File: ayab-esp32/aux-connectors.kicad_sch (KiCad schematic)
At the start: 31 parts, among them J403 AYAB_I2C, J403 USER_I2C, J403 USER_UART, J404 AYAB_SPI, J404 USER_SPI

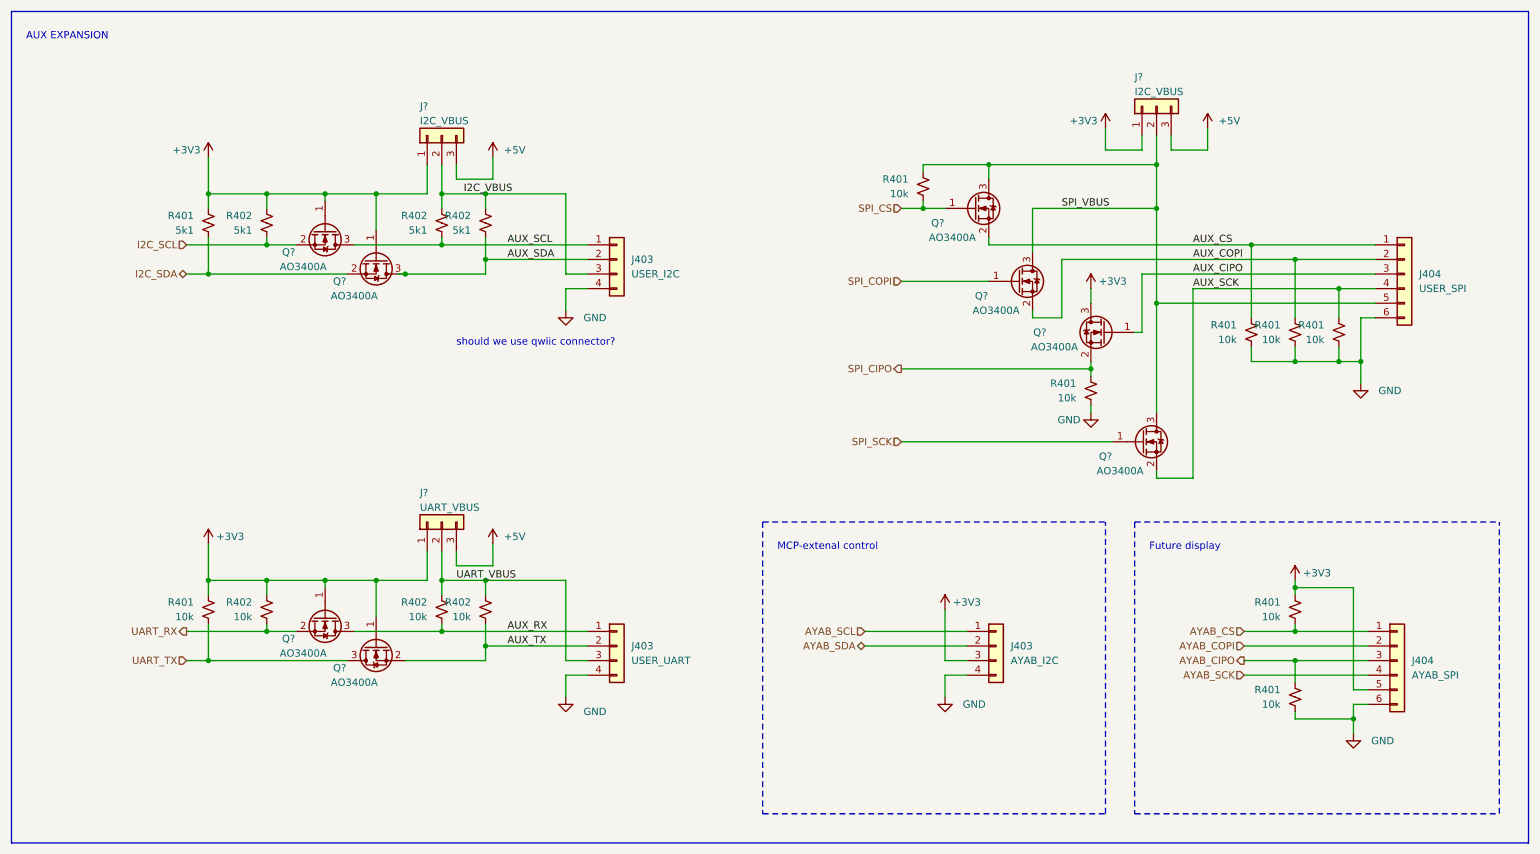
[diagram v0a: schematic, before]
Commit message: annotate and terminating resistors
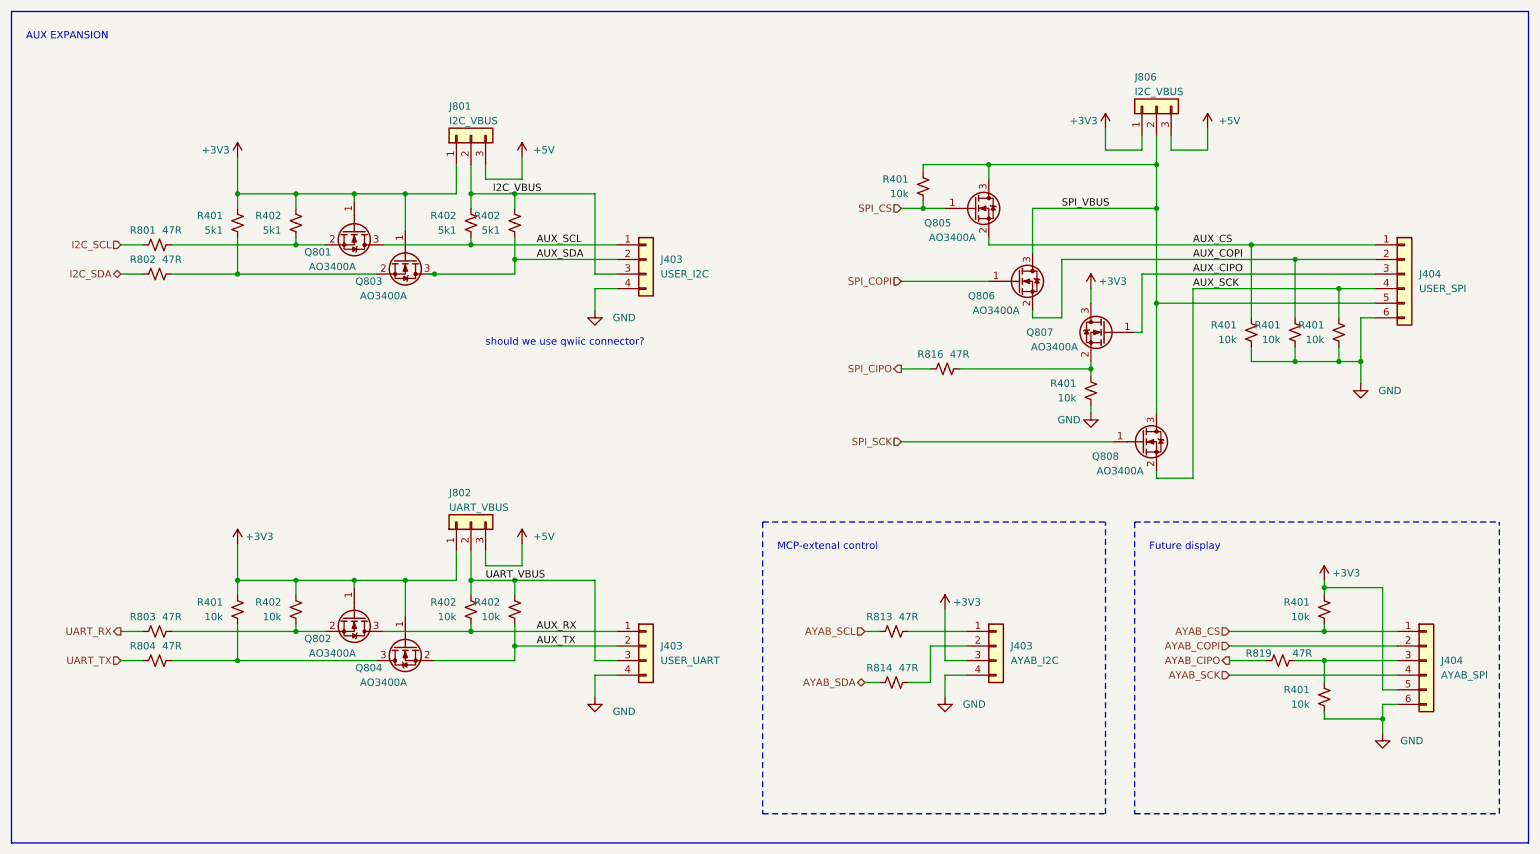
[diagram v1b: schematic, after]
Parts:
- added R801, R802, R803, R804, R813, R814, R816, R819: 47R, symbol ayab-esp32:R_Small_US
- gave numbers to parts that had none: 11
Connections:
- net AYAB_CIPO: now also R819.1; no longer J404.3 (Pin_3), R401.1
- net AYAB_SCL: now also R813.1; no longer J403.1 (Pin_1)
- net AYAB_SDA: now also R814.1; no longer J403.2 (Pin_2)
- net I2C_SCL: now also R801.1; no longer Q801.2 (S), R402.2
- net I2C_SDA: now also R802.1; no longer Q803.2 (S), R401.2
- net SPI_CIPO: now also R816.1; no longer Q807.2 (S), R401.1
- net UART_RX: now also R803.1; no longer Q802.2 (S), R402.2
- net UART_TX: now also R804.1; no longer Q804.3 (D), R401.2
- new net: Q802.2 (S), R402.2, R803.2
- new net: J404.3 (Pin_3), R401.1, R819.2
- new net: Q807.2 (S), R401.1, R816.2
- new net: J403.1 (Pin_1), R813.2
- new net: Q804.3 (D), R401.2, R804.2
- new net: J403.2 (Pin_2), R814.2
- new net: Q801.2 (S), R402.2, R801.2
- new net: Q803.2 (S), R401.2, R802.2
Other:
- moved on the sheet: J403, J404, J801, J802, Q801, Q802, Q803, Q804, R401, R402

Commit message: finalize external connectors
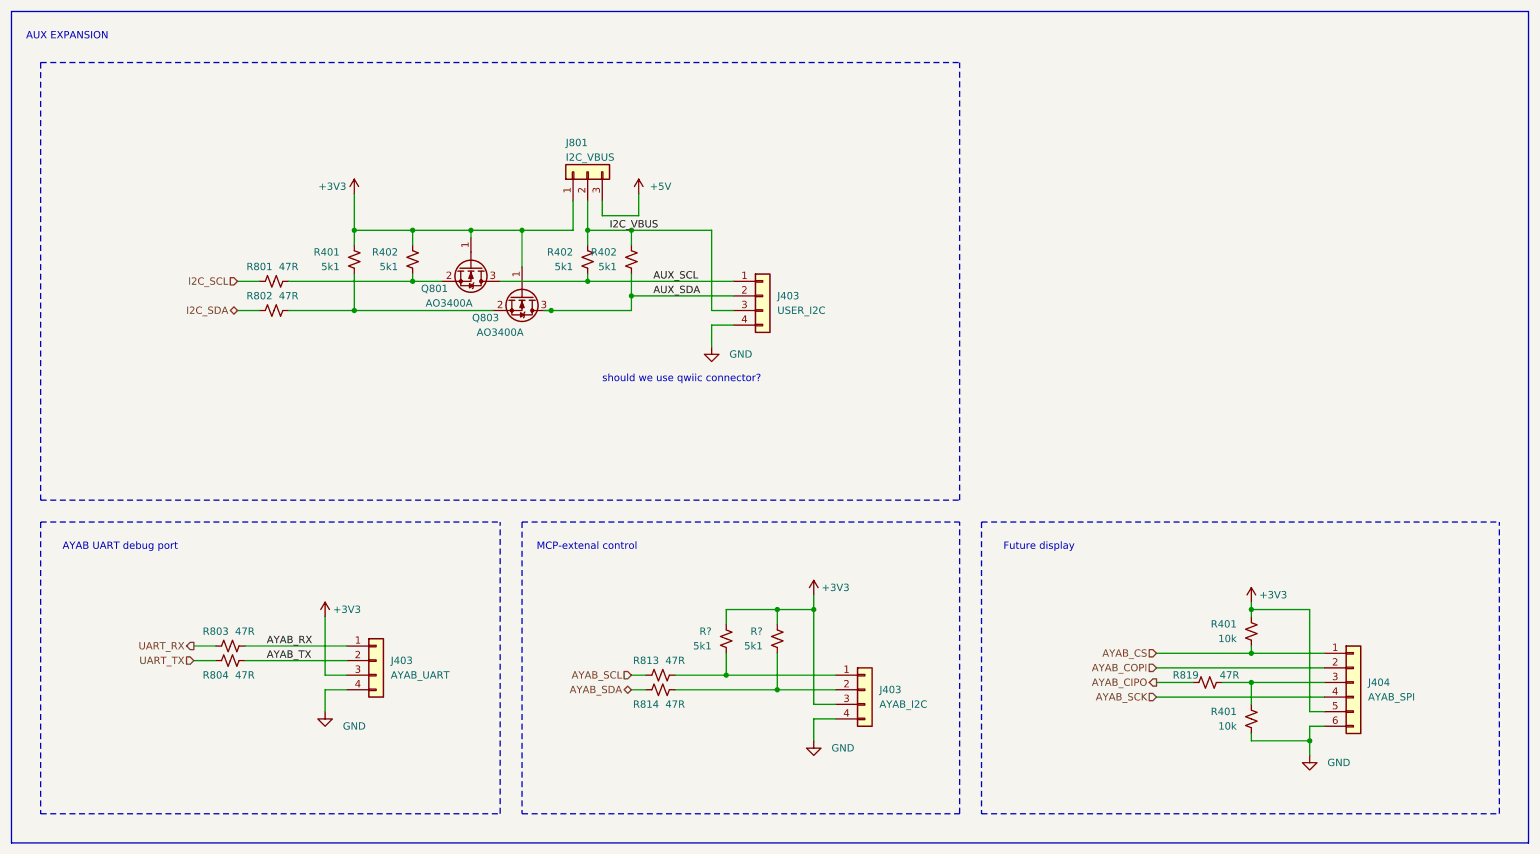
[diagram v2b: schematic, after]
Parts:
- removed J404: USER_SPI, symbol ayab-esp32:Conn_01x06
- removed J802: UART_VBUS, symbol Connector_Generic:Conn_01x03
- removed J806: I2C_VBUS, symbol Connector_Generic:Conn_01x03
- removed Q802, Q804, Q805, Q806, Q807, Q808: AO3400A, Package_TO_SOT_SMD:SOT-23, symbol ayab-esp32:AO3400A
- removed R401 (x6), R402 (x3): 10k, symbol ayab-esp32:R_Small_US
- removed R816: 47R, symbol ayab-esp32:R_Small_US
- added R? (x2): 5k1, symbol ayab-esp32:R_Small_US
- J403: value USER_UART -> AYAB_UART
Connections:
- net AUX_RX is gone; now on net AYAB_RX: J403.1 (Pin_1)
- net UART_VBUS is gone; now on net +3V3: J403.3 (Pin_3)
- net +3V3: now also R?.1, R?.1
- net AYAB_SDA: now also R814.2; no longer R814.1
- net UART_TX: now also R804.2; no longer R804.1
- net AYAB_RX: now reaches R803.2
- net at J403.1 (Pin_1), R813.2: now also R?.2
- net at J403.2 (Pin_2): now also R814.1, R?.2; no longer R814.2
- net AUX_TX renamed AYAB_TX
- net AYAB_TX: now also R804.1
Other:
- note added: "AYAB UART debug port"
- moved on the sheet: J403, J404, J801, Q801, Q803, R401, R402, R801, R802, R803, R804, R813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

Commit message: update local library + pdf
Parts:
- J802: renamed from J801; symbol Connector_Generic:Conn_01x03 -> ayab-esp32:Conn_01x03
- gave numbers to parts that had none: 2
- renumbered Q803 to Q802, R803 to R801, R804 to R802, R801 to R803, R802 to R804, R813 to R809, R814 to R810, R819 to R813

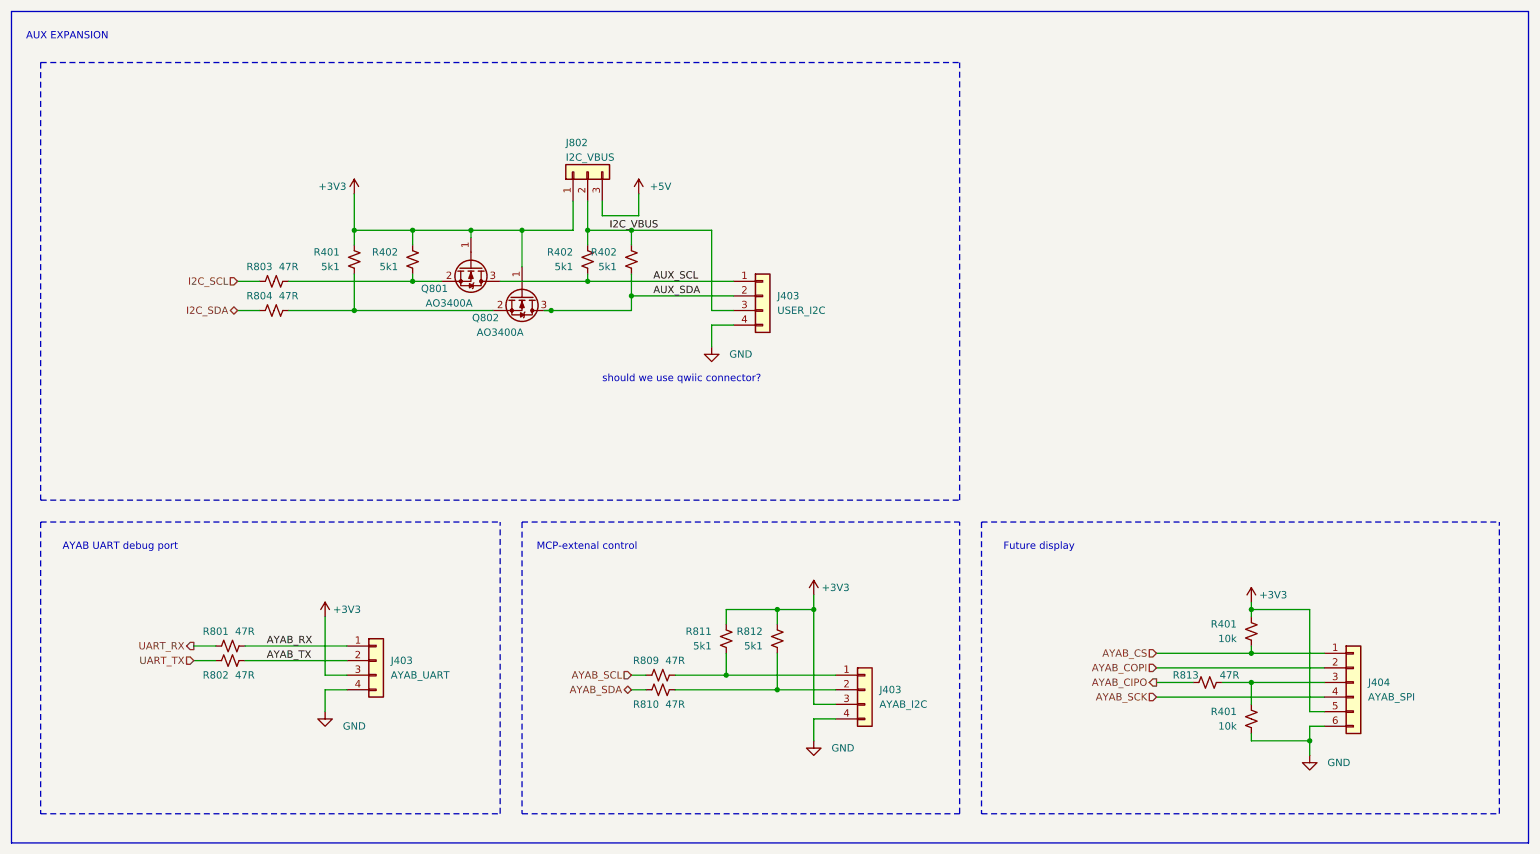
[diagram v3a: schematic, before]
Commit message: add component selection, bom
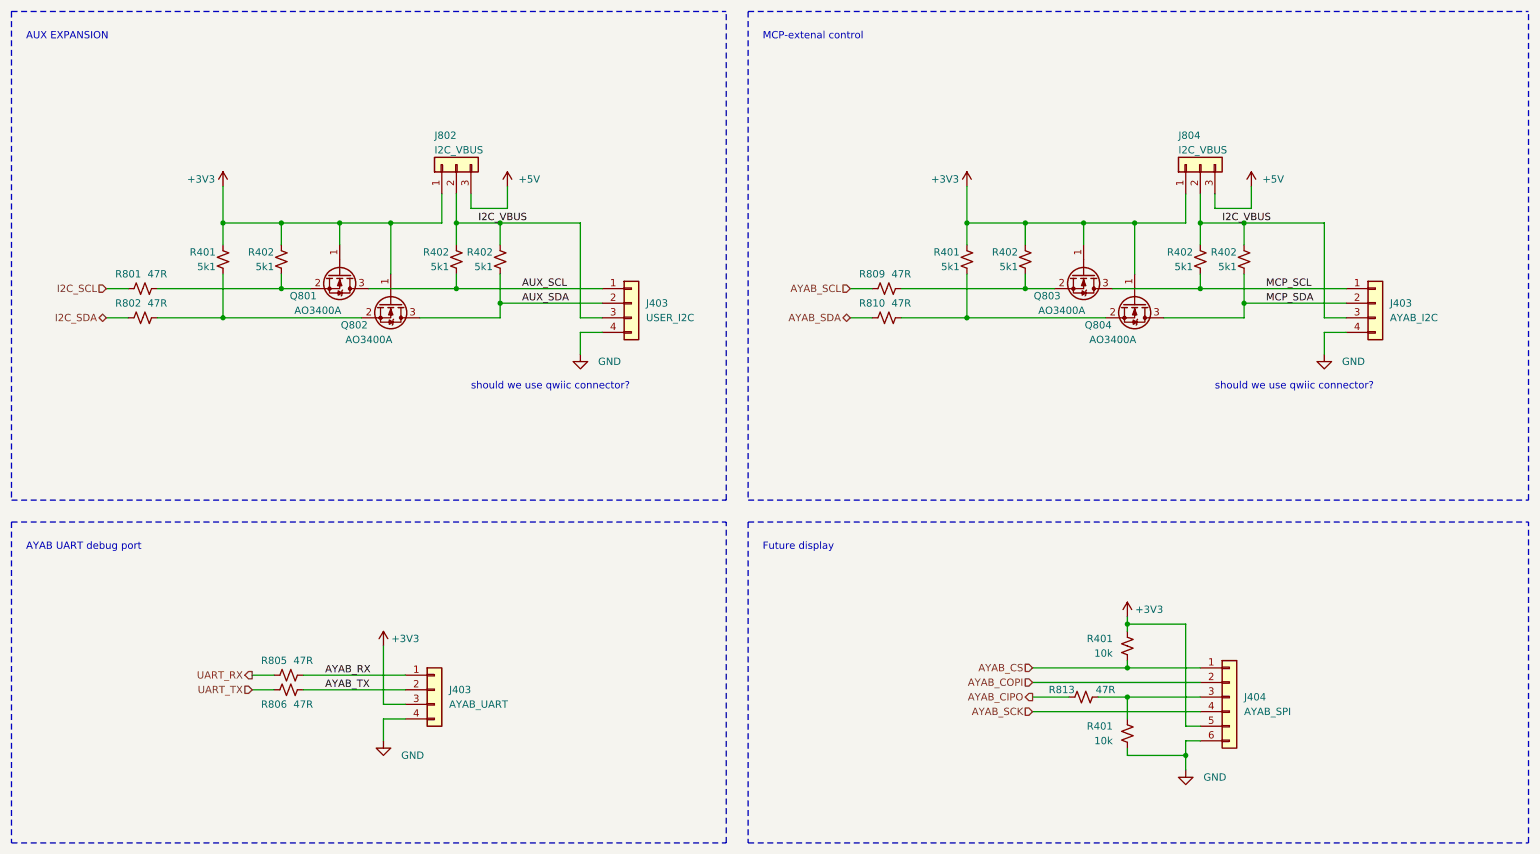
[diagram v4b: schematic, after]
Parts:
- removed R809, R810: 47R, symbol ayab-esp32:R_Small_US
- removed R811, R812: 5k1, symbol ayab-esp32:R_Small_US
- added J804: I2C_VBUS, Jumper:SolderJumper-3_P1.3mm_Bridged12_RoundedPad1.0x1.5mm, symbol Library:Conn_01x03
- added Q803, Q804: AO3400A, Package_TO_SOT_SMD:SOT-23, symbol Library:AO3400A
- added R401, R402 (x3): 5k1, Resistor_SMD:R_0603_1608Metric, symbol Library:R_Small_US
- added R809, R810: 47R, Resistor_SMD:R_0603_1608Metric, symbol Library:R_Small_US
- J403: footprint (none) -> Connector_PinHeader_2.54mm:PinHeader_1x04_P2.54mm_Vertical; symbol ayab-esp32:Conn_01x04 -> Library:Conn_01x04; LCSC ID (none) -> C3029334; OEM (none) -> XUNPU; OEM PN (none) -> WAFER-SH1.0-4PLB
- J403: footprint (none) -> Connector_JST:JST_SH_SM04B-SRSS-TB_1x04-1MP_P1.00mm_Horizontal; symbol ayab-esp32:Conn_01x04 -> Library:Conn_01x04; LCSC ID (none) -> C3029334; OEM (none) -> XUNPU; OEM PN (none) -> WAFER-SH1.0-4PLB
- J403: footprint (none) -> Connector_PinSocket_2.54mm:PinSocket_1x04_P2.54mm_Vertical; symbol ayab-esp32:Conn_01x04 -> Library:Conn_01x04; LCSC ID (none) -> C3029334; OEM (none) -> XUNPU; OEM PN (none) -> WAFER-SH1.0-4PLB
- J404: footprint (none) -> Connector_JST:JST_SH_SM06B-SRSS-TB_1x06-1MP_P1.00mm_Horizontal; symbol ayab-esp32:Conn_01x06 -> Library:Conn_01x06; LCSC ID (none) -> C3029345; OEM (none) -> XUNPU; OEM PN (none) -> WAFER-SH1.0-6PWB
- J802: footprint (none) -> Jumper:SolderJumper-3_P1.3mm_Bridged12_RoundedPad1.0x1.5mm; symbol ayab-esp32:Conn_01x03 -> Library:Conn_01x03
- Q801, Q802: symbol ayab-esp32:AO3400A -> Library:AO3400A; LCSC ID (none) -> C20917; OEM (none) -> Alpha & Omega Semicon; OEM PN (none) -> AO3400A; Package (none) -> SOT-23
- R401: footprint (none) -> Resistor_SMD:R_0603_1608Metric; symbol ayab-esp32:R_Small_US -> Library:R_Small_US; LCSC ID (none) -> C25804; OEM (none) -> UNI-ROYAL(Uniroyal Elec); OEM PN (none) -> 0603WAF1002T5E; Package (none) -> 0603
- R401, R402: footprint (none) -> Resistor_SMD:R_0603_1608Metric; symbol ayab-esp32:R_Small_US -> Library:R_Small_US; LCSC ID (none) -> C23186; OEM (none) -> UNI-ROYAL(Uniroyal Elec); OEM PN (none) -> 0603WAF5101T5E; Package (none) -> 0603
- R801: renamed from R803; footprint (none) -> Resistor_SMD:R_0603_1608Metric; symbol ayab-esp32:R_Small_US -> Library:R_Small_US; LCSC ID (none) -> C23182; OEM (none) -> UNI-ROYAL(Uniroyal Elec); OEM PN (none) -> 0603WAF470JT5E; Package (none) -> 0603
- R802: renamed from R804; footprint (none) -> Resistor_SMD:R_0603_1608Metric; symbol ayab-esp32:R_Small_US -> Library:R_Small_US; LCSC ID (none) -> C23182; OEM (none) -> UNI-ROYAL(Uniroyal Elec); OEM PN (none) -> 0603WAF470JT5E; Package (none) -> 0603
- R805: renamed from R801; footprint (none) -> Resistor_SMD:R_0603_1608Metric; symbol ayab-esp32:R_Small_US -> Library:R_Small_US; LCSC ID (none) -> C23182; OEM (none) -> UNI-ROYAL(Uniroyal Elec); OEM PN (none) -> 0603WAF470JT5E; Package (none) -> 0603
- R806: renamed from R802; footprint (none) -> Resistor_SMD:R_0603_1608Metric; symbol ayab-esp32:R_Small_US -> Library:R_Small_US; LCSC ID (none) -> C23182; OEM (none) -> UNI-ROYAL(Uniroyal Elec); OEM PN (none) -> 0603WAF470JT5E; Package (none) -> 0603
- R813: footprint (none) -> Resistor_SMD:R_0603_1608Metric; symbol ayab-esp32:R_Small_US -> Library:R_Small_US; LCSC ID (none) -> C23182; OEM (none) -> UNI-ROYAL(Uniroyal Elec); OEM PN (none) -> 0603WAF470JT5E; Package (none) -> 0603
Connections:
- net +3V3: now also J804.1 (Pin_1), Q803.1 (G), Q804.1 (G), R401.1, R402.1; no longer J403.3 (Pin_3)
- net +5V: now also J804.3 (Pin_3)
- net AYAB_SCL: now also R809.1
- net AYAB_SDA: now also R810.1
- net I2C_VBUS: now also J403.3 (Pin_3), J804.2 (Pin_2), R402.1, R402.1
- net MCP_SDA: now reaches J403.2 (Pin_2)
- net MCP_SDA: now also Q804.3 (D), R402.2
- net MCP_SCL: now reaches J403.1 (Pin_1)
- net MCP_SCL: now also Q803.3 (D), R402.2
- new net: Q804.2 (S), R401.2, R810.2
- new net: Q803.2 (S), R402.2, R809.2
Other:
- moved on the sheet: J403, J404, J802, Q801, Q802, R401, R402, R801, R802, R805, R806, R813
